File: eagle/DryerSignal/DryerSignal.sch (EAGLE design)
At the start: 18 parts, among them J1 4.5v, P1 INPUT, T1 2N3904, U1 MCP1755T-3302E/OT, U2 ATTINY85

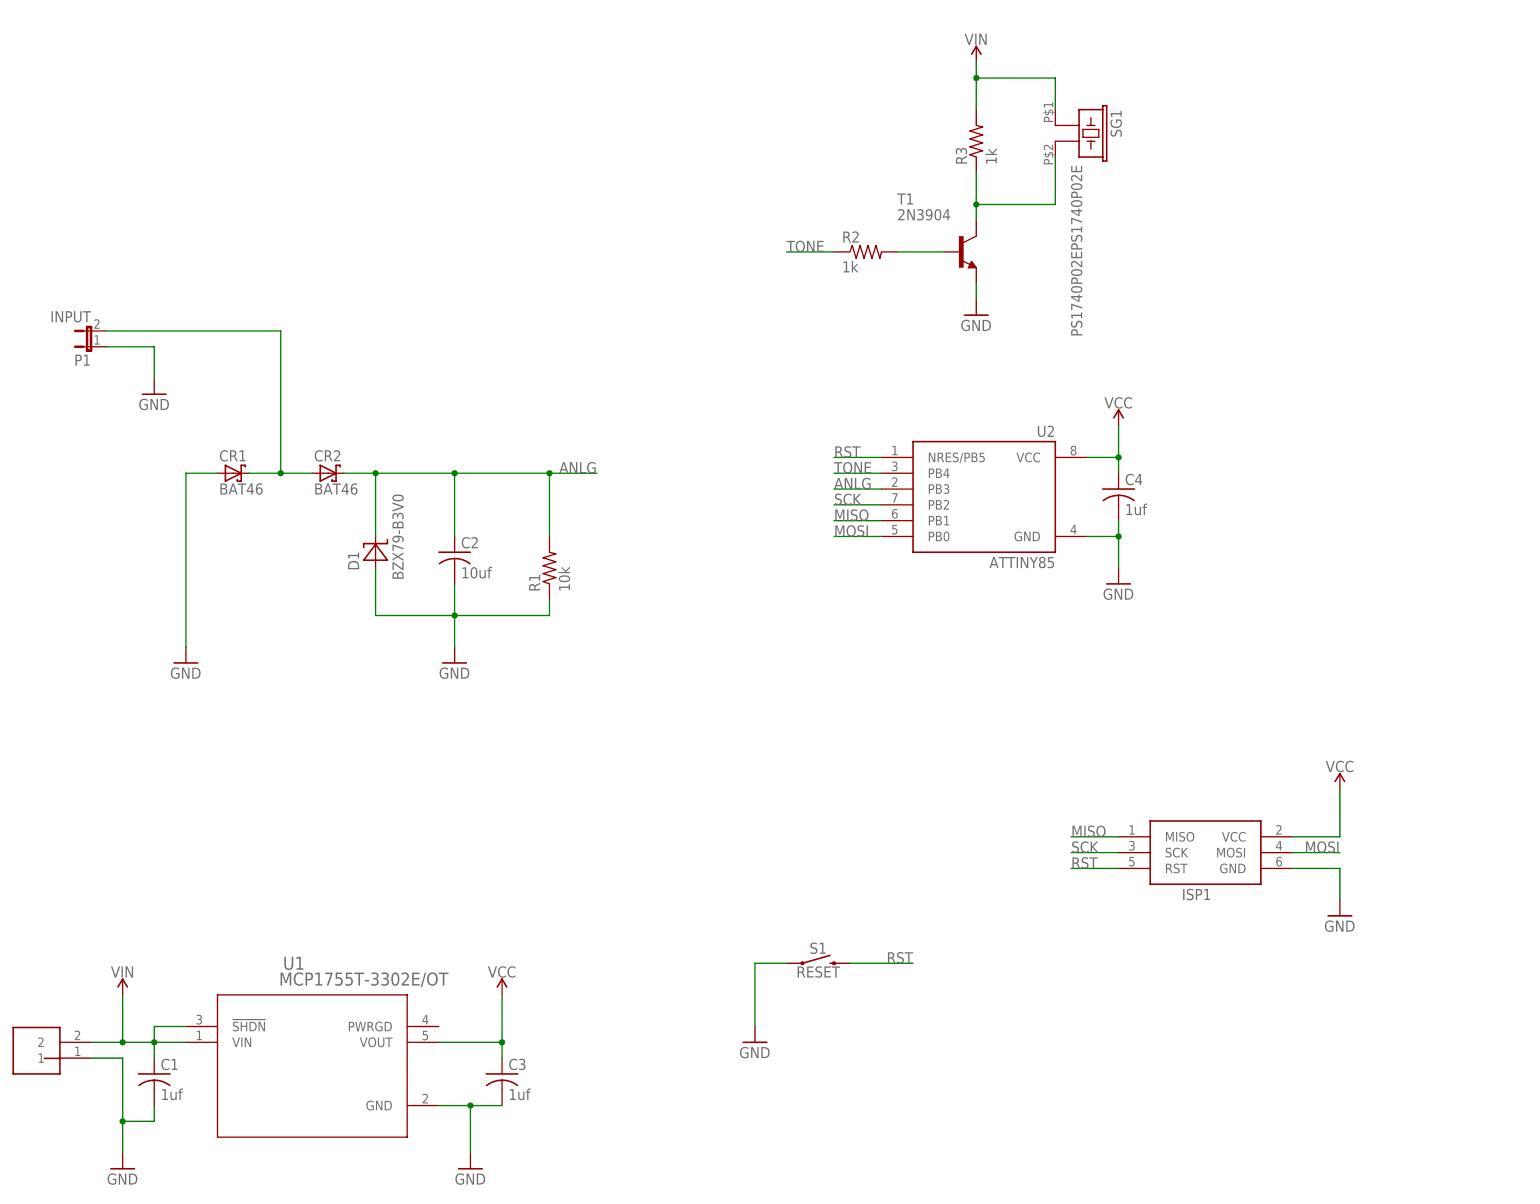
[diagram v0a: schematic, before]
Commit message: updated schematic & board to remove voltage regulator
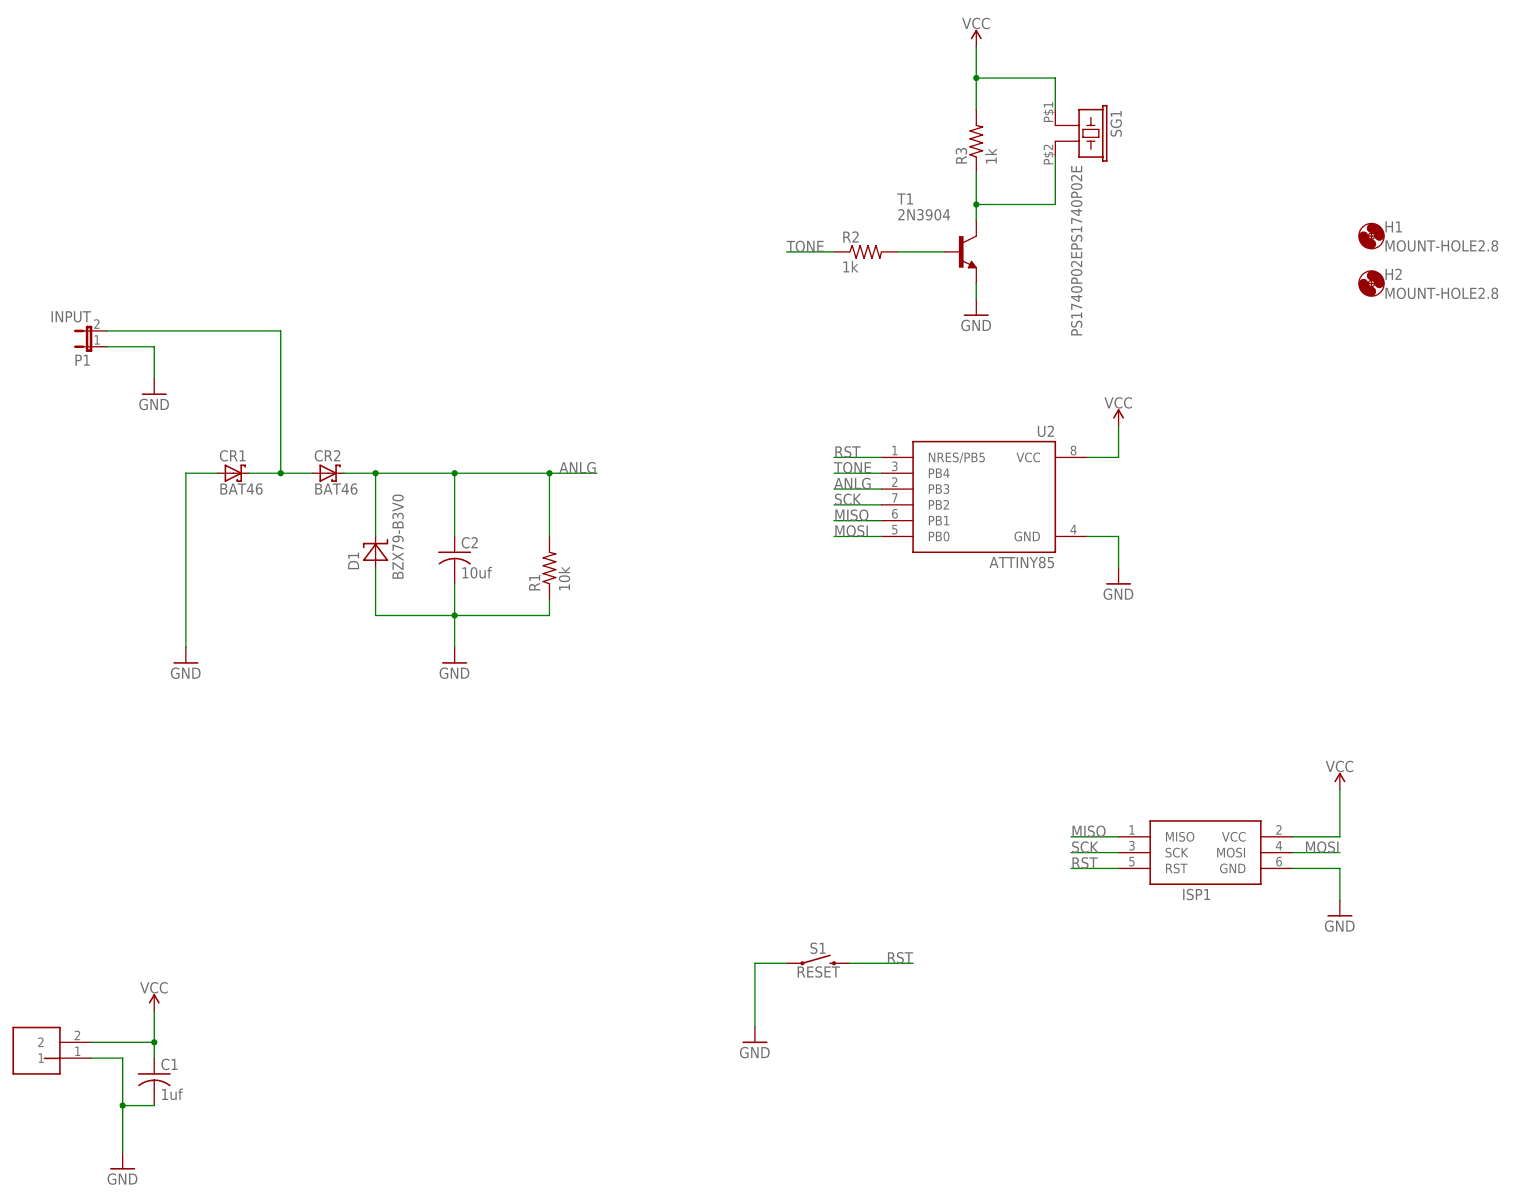
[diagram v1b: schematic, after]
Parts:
- removed C3, C4: 1uf, DryerSignal:C-US050-025X075
- removed U1: MCP1755T-3302E/OT, DryerSignal:MCP1755T-3302E/OT
- added H1, H2: MOUNT-HOLE2.8, DryerSignal:MOUNT-HOLE2.8
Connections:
- removed net VIN: C1.1, J1.2, R3.2, SG1.1, U1.!SHDN, U1.VIN
- net GND: no longer C3.2, C4.2, U1.GND
- net VCC: now also C1.1, J1.2, R3.2, SG1.1; no longer C3.1, C4.1, U1.VOUT
